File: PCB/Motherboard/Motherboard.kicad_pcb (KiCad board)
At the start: 2 copper layers, 66 x 75 mm, 16 parts, among them J10 Power, J11 QWIIC, J12 Conn_01x04_Socket, J2 North PWM, J3 South PWM, J4 East PWM, J5 West PWM, J6 North HALL, J7 South Hall, J8 East Hall, J9 West Hall

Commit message: pcb tweaks and new gerbers
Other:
- board text added: "DESIGNED BY SHAWN MALLUWA-WADU"
- board text added: "SHAWNMALLUWAWADU@GMAIL.COM"

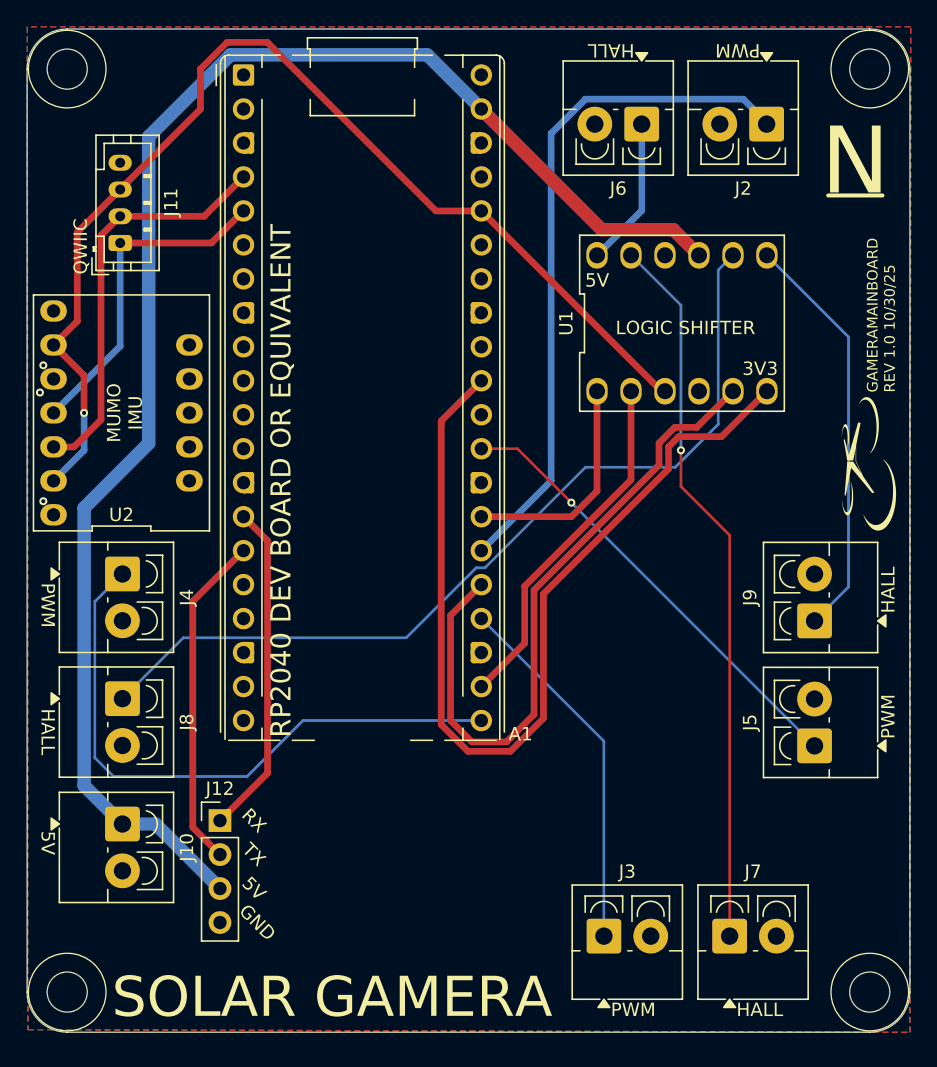
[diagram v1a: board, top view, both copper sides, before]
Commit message: refactored src for avionics with new things
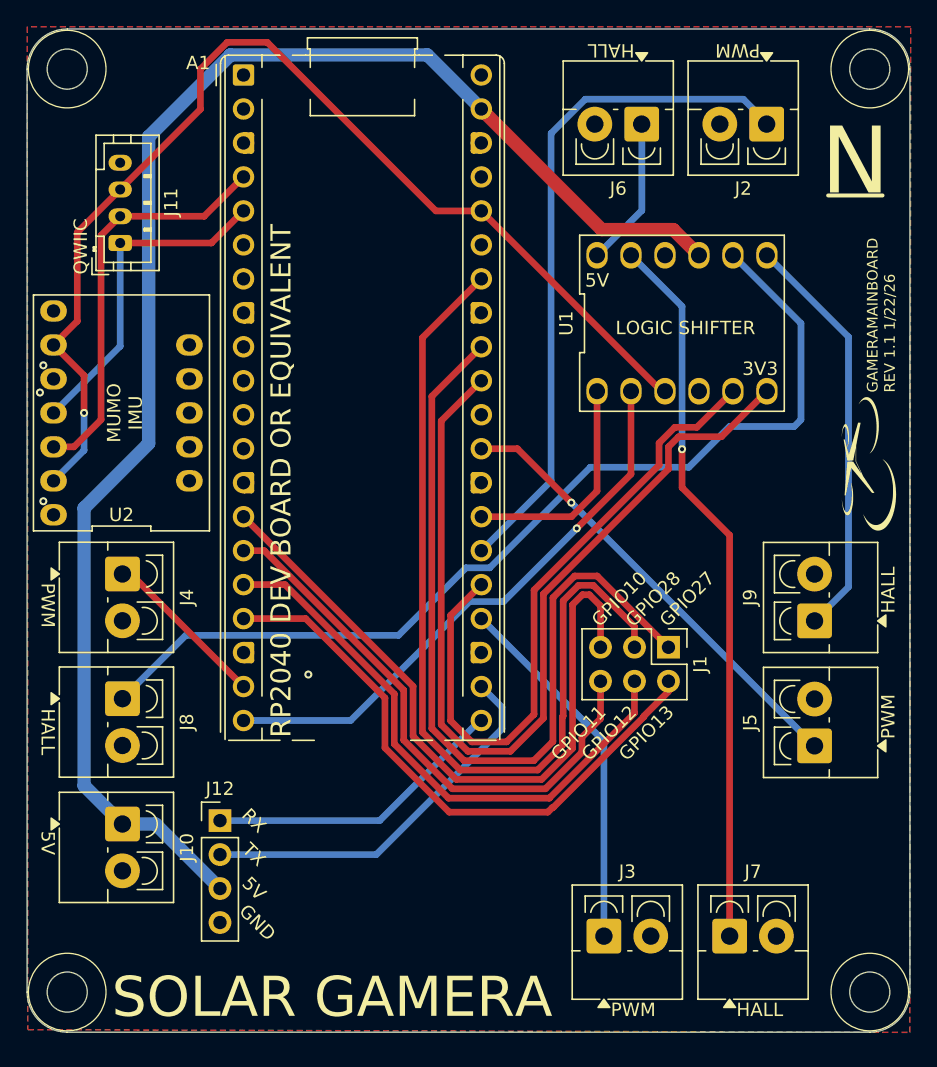
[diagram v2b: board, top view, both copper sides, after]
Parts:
- added J1: Conn_02x03_Odd_Even, Connector_PinHeader_2.54mm:PinHeader_2x03_P2.54mm_Vertical, F.Cu at (147.0, 136.2)
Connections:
- A1 pad 14: RX -> TP4
- A1 pad 15: TX -> TP3
- A1 pad 16: unconnected-(A1-GPIO12-Pad16) -> TP2
- A1 pad 17: unconnected-(A1-GPIO13-Pad17) -> TP1
- A1 pad 19: unconnected-(A1-GPIO14-Pad19) -> EPWM
- A1 pad 20: unconnected-(A1-GPIO15-Pad20) -> EHALL3V3
- A1 pad 21: EPWM -> RX
- A1 pad 22: EHALL3V3 -> TX
- A1 pad 32: unconnected-(A1-GPIO27_ADC1-Pad32) -> TP5
- A1 pad 34: unconnected-(A1-GPIO28_ADC2-Pad34) -> TP6
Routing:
- net TP6: track 0.00 -> 67.6 mm
- net TP5: track 0.00 -> 63.0 mm
- net TP4: track 0.00 -> 52.5 mm
- net TP1: track 0.00 -> 44.5 mm
- net TP2: track 0.00 -> 43.0 mm
- net TP3: track 0.00 -> 41.9 mm
- net EPWM: track 45.8 -> 12.5 mm
- net EHALL3V3: track 26.7 -> 42.8 mm, vias 0 -> 1
- net EHALL5V: track 66.1 -> 73.8 mm
- net TX: track 25.1 -> 28.8 mm
- net RX: track 24.9 -> 22.6 mm
- net GND: vias 3 -> 4
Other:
- board text added: "GAMERAMAINBOARD REV 1.1 1/22/26"
- board text added: "GPIO10"
- board text added: "GPIO11"
- board text added: "GPIO12"
- board text added: "GPIO13"
- board text added: "GPIO27"
- board text added: "GPIO28"
- board text removed: "GAMERAMAINBOARD REV 1.0 10/30/25"
